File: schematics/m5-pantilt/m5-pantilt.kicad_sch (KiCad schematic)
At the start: 33 parts, among them J1 Conn_02x15_Odd_Even, J2 Conn_02x15_Odd_Even, J3 Conn_01x03, J4 Conn_01x04, J5 BAT, J6 Conn_01x04, J7 5V_POWER, J8 Conn_01x03, Q1 IRLML6402, Q2 2SA1015, SW1 SW_SPDT, U1 MAX3485

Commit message: WIP: Refine board
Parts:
- C1, C2, C3, C4: footprint Capacitor_SMD:C_1206_3216Metric_Pad1.42x1.75mm_HandSolder -> Capacitor_SMD:C_1206_3216Metric_Pad1.33x1.80mm_HandSolder
- Q2: footprint Package_TO_SOT_THT:TO-92_Inline -> Package_TO_SOT_SMD:SOT-23
- R10, R11, R12, R13, R14, R3, R4, R5, R9: footprint Resistor_SMD:R_0603_1608Metric_Pad1.05x0.95mm_HandSolder -> Resistor_SMD:R_0603_1608Metric_Pad0.98x0.95mm_HandSolder
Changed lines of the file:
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@@
       (effects (font (size 1.27 1.27)) (justify left))
     )
-    (property "Footprint" "Resistor_SMD:R_0603_1608Metric_Pad1.05x0.95mm_HandSolder" (id 2) (at 205.74 97.282 90)
+    (property "Footprint" "Resistor_SMD:R_0603_1608Metric_Pad0.98x0.95mm_HandSolder" (id 2) (at 205.74 97.282 90)
       (effects (font (size 1.27 1.27)) hide)
     )
@@
       (effects (font (size 1.27 1.27)) (justify left))
     )
-    (property "Footprint" "Resistor_SMD:R_0603_1608Metric_Pad1.05x0.95mm_HandSolder" (id 2) (at 205.74 123.952 90)
+    (property "Footprint" "Resistor_SMD:R_0603_1608Metric_Pad0.98x0.95mm_HandSolder" (id 2) (at 205.74 123.952 90)
       (effects (font (size 1.27 1.27)) hide)
     )
@@
     (property "Reference" "C1" (id 0) (at 215.9 86.36 0))
     (property "Value" "100u" (id 1) (at 214.63 88.9 0))
-    (property "Footprint" "Capacitor_SMD:C_1206_3216Metric_Pad1.42x1.75mm_HandSolder" (id 2) (at 218.7448 83.82 0)
+    (property "Footprint" "Capacitor_SMD:C_1206_3216Metric_Pad1.33x1.80mm_HandSolder" (id 2) (at 218.7448 83.82 0)
       (effects (font (size 1.27 1.27)) hide)
     )
@@
     (property "Reference" "C4" (id 0) (at 215.9 111.76 0))
     (property "Value" "100u" (id 1) (at 214.63 114.3 0))
-    (property "Footprint" "Capacitor_SMD:C_1206_3216Metric_Pad1.42x1.75mm_HandSolder" (id 2) (at 218.7448 109.22 0)
+    (property "Footprint" "Capacitor_SMD:C_1206_3216Metric_Pad1.33x1.80mm_HandSolder" (id 2) (at 218.7448 109.22 0)
       (effects (font (size 1.27 1.27)) hide)
     )
@@
       (effects (font (size 1.27 1.27)) (justify right))
     )
-    (property "Footprint" "Resistor_SMD:R_0603_1608Metric_Pad1.05x0.95mm_HandSolder" (id 2) (at 36.068 143.51 90)
+    (property "Footprint" "Resistor_SMD:R_0603_1608Metric_Pad0.98x0.95mm_HandSolder" (id 2) (at 36.068 143.51 90)
       (effects (font (size 1.27 1.27)) hide)
     )
@@
     (property "Reference" "C2" (id 0) (at 204.47 86.36 0))
     (property "Value" "100u" (id 1) (at 203.2 88.9 0))
-    (property "Footprint" "Capacitor_SMD:C_1206_3216Metric_Pad1.42x1.75mm_HandSolder" (id 2) (at 207.3148 83.82 0)
+    (property "Footprint" "Capacitor_SMD:C_1206_3216Metric_Pad1.33x1.80mm_HandSolder" (id 2) (at 207.3148 83.82 0)
       (effects (font (size 1.27 1.27)) hide)
     )
@@
     (property "Reference" "C3" (id 0) (at 204.47 111.76 0))
     (property "Value" "100u" (id 1) (at 203.2 114.3 0))
-    (property "Footprint" "Capacitor_SMD:C_1206_3216Metric_Pad1.42x1.75mm_HandSolder" (id 2) (at 209.2452 116.84 0)
+    (property "Footprint" "Capacitor_SMD:C_1206_3216Metric_Pad1.33x1.80mm_HandSolder" (id 2) (at 209.2452 116.84 0)
       (effects (font (size 1.27 1.27)) hide)
     )
@@
     (property "Reference" "R9" (id 0) (at 220.98 32.8422 90))
     (property "Value" "0" (id 1) (at 220.98 35.1536 90))
-    (property "Footprint" "Resistor_SMD:R_0603_1608Metric_Pad1.05x0.95mm_HandSolder" (id 2) (at 220.98 36.322 90)
+    (property "Footprint" "Resistor_SMD:R_0603_1608Metric_Pad0.98x0.95mm_HandSolder" (id 2) (at 220.98 36.322 90)
       (effects (font (size 1.27 1.27)) hide)
     )
@@
     (property "Reference" "R10" (id 0) (at 220.98 41.7322 90))
     (property "Value" "0" (id 1) (at 220.98 44.0436 90))
-    (property "Footprint" "Resistor_SMD:R_0603_1608Metric_Pad1.05x0.95mm_HandSolder" (id 2) (at 220.98 45.212 90)
+    (property "Footprint" "Resistor_SMD:R_0603_1608Metric_Pad0.98x0.95mm_HandSolder" (id 2) (at 220.98 45.212 90)
       (effects (font (size 1.27 1.27)) hide)
     )
@@
     (property "Reference" "R11" (id 0) (at 220.98 50.6222 90))
     (property "Value" "0" (id 1) (at 220.98 52.9336 90))
-    (property "Footprint" "Resistor_SMD:R_0603_1608Metric_Pad1.05x0.95mm_HandSolder" (id 2) (at 220.98 54.102 90)
+    (property "Footprint" "Resistor_SMD:R_0603_1608Metric_Pad0.98x0.95mm_HandSolder" (id 2) (at 220.98 54.102 90)
       (effects (font (size 1.27 1.27)) hide)
     )
@@
     (property "Reference" "R12" (id 0) (at 220.98 59.5122 90))
     (property "Value" "0" (id 1) (at 220.98 61.8236 90))
-    (property "Footprint" "Resistor_SMD:R_0603_1608Metric_Pad1.05x0.95mm_HandSolder" (id 2) (at 220.98 62.992 90)
+    (property "Footprint" "Resistor_SMD:R_0603_1608Metric_Pad0.98x0.95mm_HandSolder" (id 2) (at 220.98 62.992 90)
       (effects (font (size 1.27 1.27)) hide)
     )
@@
     (property "Reference" "R13" (id 0) (at 227.33 96.52 90))
     (property "Value" "0" (id 1) (at 229.87 96.1136 90))
-    (property "Footprint" "Resistor_SMD:R_0603_1608Metric_Pad1.05x0.95mm_HandSolder" (id 2) (at 229.87 97.282 90)
+    (property "Footprint" "Resistor_SMD:R_0603_1608Metric_Pad0.98x0.95mm_HandSolder" (id 2) (at 229.87 97.282 90)
       (effects (font (size 1.27 1.27)) hide)
     )
@@
     (property "Reference" "R14" (id 0) (at 227.33 123.19 90))
     (property "Value" "0" (id 1) (at 229.87 122.7836 90))
-    (property "Footprint" "Resistor_SMD:R_0603_1608Metric_Pad1.05x0.95mm_HandSolder" (id 2) (at 229.87 123.952 90)
+    (property "Footprint" "Resistor_SMD:R_0603_1608Metric_Pad0.98x0.95mm_HandSolder" (id 2) (at 229.87 123.952 90)
       (effects (font (size 1.27 1.27)) hide)
     )
@@
       (effects (font (size 1.27 1.27)) (justify left))
     )
-    (property "Footprint" "Package_TO_SOT_THT:TO-92_Inline" (id 2) (at 97.79 131.445 0)
+    (property "Footprint" "Package_TO_SOT_SMD:SOT-23" (id 2) (at 97.79 131.445 0)
       (effects (font (size 1.27 1.27) italic) (justify left) hide)
     )
@@
     )
     (path "/00000000-0000-0000-0000-000060cb98bd"
-      (reference "C1") (unit 1) (value "100u") (footprint "Capacitor_SMD:C_1206_3216Metric_Pad1.42x1.75mm_HandSolder")
+      (reference "C1") (unit 1) (value "100u") (footprint "Capacitor_SMD:C_1206_3216Metric_Pad1.33x1.80mm_HandSolder")
     )
     (path "/00000000-0000-0000-0000-000061ea93dc"
-      (reference "C2") (unit 1) (value "100u") (footprint "Capacitor_SMD:C_1206_3216Metric_Pad1.42x1.75mm_HandSolder")
+      (reference "C2") (unit 1) (value "100u") (footprint "Capacitor_SMD:C_1206_3216Metric_Pad1.33x1.80mm_HandSolder")
     )
     (path "/00000000-0000-0000-0000-000061eb9195"
-      (reference "C3") (unit 1) (value "100u") (footprint "Capacitor_SMD:C_1206_3216Metric_Pad1.42x1.75mm_HandSolder")
+      (reference "C3") (unit 1) (value "100u") (footprint "Capacitor_SMD:C_1206_3216Metric_Pad1.33x1.80mm_HandSolder")
     )
     (path "/00000000-0000-0000-0000-000061dd33e8"
-      (reference "C4") (unit 1) (value "100u") (footprint "Capacitor_SMD:C_1206_3216Metric_Pad1.42x1.75mm_HandSolder")
+      (reference "C4") (unit 1) (value "100u") (footprint "Capacitor_SMD:C_1206_3216Metric_Pad1.33x1.80mm_HandSolder")
     )
     (path "/00000000-0000-0000-0000-000064ba5a4b"
@@
     )
     (path "/00000000-0000-0000-0000-000064bdb211"
-      (reference "Q2") (unit 1) (value "2SA1015") (footprint "Package_TO_SOT_THT:TO-92_Inline")
+      (reference "Q2") (unit 1) (value "2SA1015") (footprint "Package_TO_SOT_SMD:SOT-23")
     )
     (path "/202ce841-9799-487b-99b7-75e313de629f"
@@
     )
     (path "/00000000-0000-0000-0000-000060c80000"
-      (reference "R3") (unit 1) (value "1k") (footprint "Resistor_SMD:R_0603_1608Metric_Pad1.05x0.95mm_HandSolder")
+      (reference "R3") (unit 1) (value "1k") (footprint "Resistor_SMD:R_0603_1608Metric_Pad0.98x0.95mm_HandSolder")
     )
     (path "/00000000-0000-0000-0000-000060c8863a"
-      (reference "R4") (unit 1) (value "1k") (footprint "Resistor_SMD:R_0603_1608Metric_Pad1.05x0.95mm_HandSolder")
+      (reference "R4") (unit 1) (value "1k") (footprint "Resistor_SMD:R_0603_1608Metric_Pad0.98x0.95mm_HandSolder")
     )
     (path "/00000000-0000-0000-0000-000061dec6ed"
-      (reference "R5") (unit 1) (value "47k") (footprint "Resistor_SMD:R_0603_1608Metric_Pad1.05x0.95mm_HandSolder")
+      (reference "R5") (unit 1) (value "47k") (footprint "Resistor_SMD:R_0603_1608Metric_Pad0.98x0.95mm_HandSolder")
     )
     (path "/d5da4752-cd55-4f6d-aea2-a0a9d2d835e7"
@@
     )
     (path "/00000000-0000-0000-0000-000062f00fd0"
-      (reference "R9") (unit 1) (value "0") (footprint "Resistor_SMD:R_0603_1608Metric_Pad1.05x0.95mm_HandSolder")
+      (reference "R9") (unit 1) (value "0") (footprint "Resistor_SMD:R_0603_1608Metric_Pad0.98x0.95mm_HandSolder")
     )
     (path "/00000000-0000-0000-0000-000062f2bcba"
-      (reference "R10") (unit 1) (value "0") (footprint "Resistor_SMD:R_0603_1608Metric_Pad1.05x0.95mm_HandSolder")
+      (reference "R10") (unit 1) (value "0") (footprint "Resistor_SMD:R_0603_1608Metric_Pad0.98x0.95mm_HandSolder")
     )
     (path "/00000000-0000-0000-0000-000062f42c81"
-      (reference "R11") (unit 1) (value "0") (footprint "Resistor_SMD:R_0603_1608Metric_Pad1.05x0.95mm_HandSolder")
+      (reference "R11") (unit 1) (value "0") (footprint "Resistor_SMD:R_0603_1608Metric_Pad0.98x0.95mm_HandSolder")
     )
     (path "/00000000-0000-0000-0000-000062f4da9d"
-      (reference "R12") (unit 1) (value "0") (footprint "Resistor_SMD:R_0603_1608Metric_Pad1.05x0.95mm_HandSolder")
+      (reference "R12") (unit 1) (value "0") (footprint "Resistor_SMD:R_0603_1608Metric_Pad0.98x0.95mm_HandSolder")
     )
     (path "/00000000-0000-0000-0000-000062f8bb17"
-      (reference "R13") (unit 1) (value "0") (footprint "Resistor_SMD:R_0603_1608Metric_Pad1.05x0.95mm_HandSolder")
+      (reference "R13") (unit 1) (value "0") (footprint "Resistor_SMD:R_0603_1608Metric_Pad0.98x0.95mm_HandSolder")
     )
     (path "/00000000-0000-0000-0000-000062f969a1"
-      (reference "R14") (unit 1) (value "0") (footprint "Resistor_SMD:R_0603_1608Metric_Pad1.05x0.95mm_HandSolder")
+      (reference "R14") (unit 1) (value "0") (footprint "Resistor_SMD:R_0603_1608Metric_Pad0.98x0.95mm_HandSolder")
     )
     (path "/00000000-0000-0000-0000-000064ba6374"

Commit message: WIP: update board
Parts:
- J3, J8: footprint Connector_PinHeader_2.54mm:PinHeader_1x03_P2.54mm_Vertical -> Connector_JST:JST_EH_B3B-EH-A_1x03_P2.50mm_Vertical
- Q2: footprint Package_TO_SOT_SMD:SOT-23 -> m5-pantilt:2SA1015_SOT-23
- R13, R14: footprint Resistor_SMD:R_0603_1608Metric_Pad0.98x0.95mm_HandSolder -> Resistor_SMD:R_0603_1608Metric
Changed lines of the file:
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@@
     (property "Reference" "R13" (id 0) (at 227.33 96.52 90))
     (property "Value" "0" (id 1) (at 229.87 96.1136 90))
-    (property "Footprint" "Resistor_SMD:R_0603_1608Metric_Pad0.98x0.95mm_HandSolder" (id 2) (at 229.87 97.282 90)
+    (property "Footprint" "Resistor_SMD:R_0603_1608Metric" (id 2) (at 229.87 97.282 90)
       (effects (font (size 1.27 1.27)) hide)
     )
@@
     (property "Reference" "R14" (id 0) (at 227.33 123.19 90))
     (property "Value" "0" (id 1) (at 229.87 122.7836 90))
-    (property "Footprint" "Resistor_SMD:R_0603_1608Metric_Pad0.98x0.95mm_HandSolder" (id 2) (at 229.87 123.952 90)
+    (property "Footprint" "Resistor_SMD:R_0603_1608Metric" (id 2) (at 229.87 123.952 90)
       (effects (font (size 1.27 1.27)) hide)
     )
@@
       (effects (font (size 1.27 1.27)) (justify left))
     )
-    (property "Footprint" "Package_TO_SOT_SMD:SOT-23" (id 2) (at 97.79 131.445 0)
+    (property "Footprint" "m5-pantilt:2SA1015_SOT-23" (id 2) (at 97.79 131.445 0)
       (effects (font (size 1.27 1.27) italic) (justify left) hide)
     )
@@
       (effects (font (size 1.27 1.27)) (justify left))
     )
-    (property "Footprint" "Connector_PinHeader_2.54mm:PinHeader_1x03_P2.54mm_Vertical" (id 2) (at 248.92 109.22 0)
+    (property "Footprint" "Connector_JST:JST_EH_B3B-EH-A_1x03_P2.50mm_Vertical" (id 2) (at 248.92 109.22 0)
       (effects (font (size 1.27 1.27)) hide)
     )
@@
       (effects (font (size 1.27 1.27)) (justify left))
     )
-    (property "Footprint" "Connector_PinHeader_2.54mm:PinHeader_1x03_P2.54mm_Vertical" (id 2) (at 248.92 83.82 0)
+    (property "Footprint" "Connector_JST:JST_EH_B3B-EH-A_1x03_P2.50mm_Vertical" (id 2) (at 248.92 83.82 0)
       (effects (font (size 1.27 1.27)) hide)
     )
@@
     )
     (path "/00000000-0000-0000-0000-000064d4e0a6"
-      (reference "J3") (unit 1) (value "Conn_01x03") (footprint "Connector_PinHeader_2.54mm:PinHeader_1x03_P2.54mm_Vertical")
+      (reference "J3") (unit 1) (value "Conn_01x03") (footprint "Connector_JST:JST_EH_B3B-EH-A_1x03_P2.50mm_Vertical")
     )
     (path "/00000000-0000-0000-0000-000060ca66e1"
@@
     )
     (path "/00000000-0000-0000-0000-000064d3a231"
-      (reference "J8") (unit 1) (value "Conn_01x03") (footprint "Connector_PinHeader_2.54mm:PinHeader_1x03_P2.54mm_Vertical")
+      (reference "J8") (unit 1) (value "Conn_01x03") (footprint "Connector_JST:JST_EH_B3B-EH-A_1x03_P2.50mm_Vertical")
     )
     (path "/00000000-0000-0000-0000-000061ddc391"
@@
     )
     (path "/00000000-0000-0000-0000-000064bdb211"
-      (reference "Q2") (unit 1) (value "2SA1015") (footprint "Package_TO_SOT_SMD:SOT-23")
+      (reference "Q2") (unit 1) (value "2SA1015") (footprint "m5-pantilt:2SA1015_SOT-23")
     )
     (path "/202ce841-9799-487b-99b7-75e313de629f"
@@
     )
     (path "/00000000-0000-0000-0000-000062f8bb17"
-      (reference "R13") (unit 1) (value "0") (footprint "Resistor_SMD:R_0603_1608Metric_Pad0.98x0.95mm_HandSolder")
+      (reference "R13") (unit 1) (value "0") (footprint "Resistor_SMD:R_0603_1608Metric")
     )
     (path "/00000000-0000-0000-0000-000062f969a1"
-      (reference "R14") (unit 1) (value "0") (footprint "Resistor_SMD:R_0603_1608Metric_Pad0.98x0.95mm_HandSolder")
+      (reference "R14") (unit 1) (value "0") (footprint "Resistor_SMD:R_0603_1608Metric")
     )
     (path "/00000000-0000-0000-0000-000064ba6374"

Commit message: Update board
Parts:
- removed Q2: 2SA1015, m5-pantilt:2SA1015_SOT-23, symbol Transistor_BJT:2SA1015
- added Q2: BC857, Package_TO_SOT_SMD:SOT-23, symbol Transistor_BJT:BC857
- R2: value 7.5k -> 5k
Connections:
- net +3V3: now also Q2.2 (E)
- net at R7.1, U1.2 (~{RE}), U1.3 (DE): now also Q2.3 (C)
- net at R2.2: now also Q2.1 (B)
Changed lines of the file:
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@@
     (pin "1")
-  )
-  (symbol (lib_id "Transistor_BJT:2SA1015") (at 92.71 129.54 0) (unit 1)
-    (in_bom yes) (on_board yes)
-    (property "Reference" "Q2" (id 0) (at 97.5614 128.3716 0)
-      (effects (font (size 1.27 1.27)) (justify left))
-    )
-    (property "Value" "2SA1015" (id 1) (at 97.5614 130.683 0)
-      (effects (font (size 1.27 1.27)) (justify left))
-    )
-    (property "Footprint" "m5-pantilt:2SA1015_SOT-23" (id 2) (at 97.79 131.445 0)
-      (effects (font (size 1.27 1.27) italic) (justify left) hide)
-    )
-    (property "Datasheet" "http://www.datasheetcatalog.org/datasheet/toshiba/905.pdf" (id 3) (at 92.71 129.54 0)
-      (effects (font (size 1.27 1.27)) (justify left) hide)
-    )
-    (pin "1")
-    (pin "2")
-    (pin "3")
   )
   (symbol (lib_id "Device:R") (at 95.25 146.05 0) (unit 1)
@@
     (in_bom yes) (on_board yes) (fields_autoplaced)
     (property "Reference" "R2" (id 0) (at 81.28 123.19 90))
-    (property "Value" "7.5k" (id 1) (at 81.28 125.73 90))
+    (property "Value" "5k" (id 1) (at 81.28 125.73 90))
     (property "Footprint" "Resistor_SMD:R_0603_1608Metric" (id 2) (at 81.28 131.318 90)
       (effects (font (size 1.27 1.27)) hide)
@@
     (pin "1")
   )
+  (symbol (lib_id "Transistor_BJT:BC857") (at 92.71 129.54 0) (mirror x) (unit 1)
+    (in_bom yes) (on_board yes) (fields_autoplaced)
+    (property "Reference" "Q2" (id 0) (at 97.79 128.2699 0)
+      (effects (font (size 1.27 1.27)) (justify left))
+    )
+    (property "Value" "BC857" (id 1) (at 97.79 130.8099 0)
+      (effects (font (size 1.27 1.27)) (justify left))
+    )
+    (property "Footprint" "Package_TO_SOT_SMD:SOT-23" (id 2) (at 97.79 127.635 0)
+      (effects (font (size 1.27 1.27) italic) (justify left) hide)
+    )
+    (property "Datasheet" "https://www.onsemi.com/pub/Collateral/BC860-D.pdf" (id 3) (at 92.71 129.54 0)
+      (effects (font (size 1.27 1.27)) (justify left) hide)
+    )
+    (pin "1")
+    (pin "2")
+    (pin "3")
+  )
   (sheet_instances
     (path "/" (page "1"))
@@
       (reference "Q1") (unit 1) (value "IRLML6402") (footprint "Package_TO_SOT_SMD:SOT-23")
     )
-    (path "/00000000-0000-0000-0000-000064bdb211"
-      (reference "Q2") (unit 1) (value "2SA1015") (footprint "m5-pantilt:2SA1015_SOT-23")
+    (path "/fd72c6fd-8d01-4c84-aa64-052ccdf03377"
+      (reference "Q2") (unit 1) (value "BC857") (footprint "Package_TO_SOT_SMD:SOT-23")
     )
     (path "/202ce841-9799-487b-99b7-75e313de629f"
@@
     )
     (path "/b82df952-3fb3-4e09-9ff8-6b87cc7e46fc"
-      (reference "R2") (unit 1) (value "7.5k") (footprint "Resistor_SMD:R_0603_1608Metric")
+      (reference "R2") (unit 1) (value "5k") (footprint "Resistor_SMD:R_0603_1608Metric")
     )
     (path "/00000000-0000-0000-0000-000060c80000"

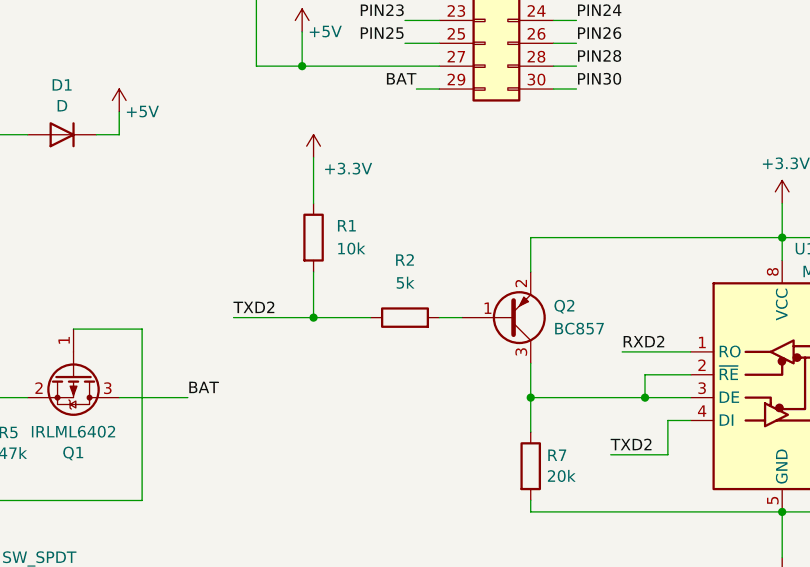
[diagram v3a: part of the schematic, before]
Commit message: 5k->5.1k
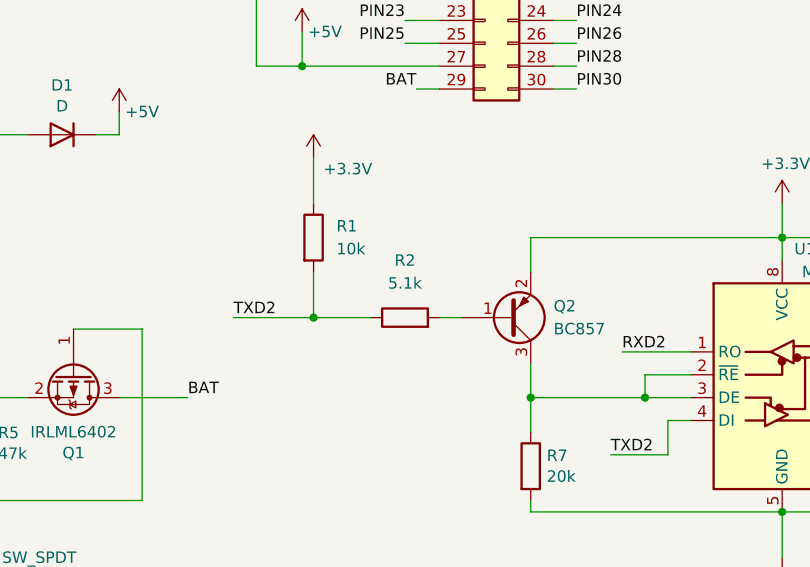
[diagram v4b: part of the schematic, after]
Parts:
- R2: value 5k -> 5.1k
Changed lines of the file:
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@@
     (in_bom yes) (on_board yes) (fields_autoplaced)
     (property "Reference" "R2" (id 0) (at 81.28 123.19 90))
-    (property "Value" "5k" (id 1) (at 81.28 125.73 90))
+    (property "Value" "5.1k" (id 1) (at 81.28 125.73 90))
     (property "Footprint" "Resistor_SMD:R_0603_1608Metric" (id 2) (at 81.28 131.318 90)
       (effects (font (size 1.27 1.27)) hide)
@@
     )
     (path "/b82df952-3fb3-4e09-9ff8-6b87cc7e46fc"
-      (reference "R2") (unit 1) (value "5k") (footprint "Resistor_SMD:R_0603_1608Metric")
+      (reference "R2") (unit 1) (value "5.1k") (footprint "Resistor_SMD:R_0603_1608Metric")
     )
     (path "/00000000-0000-0000-0000-000060c80000"

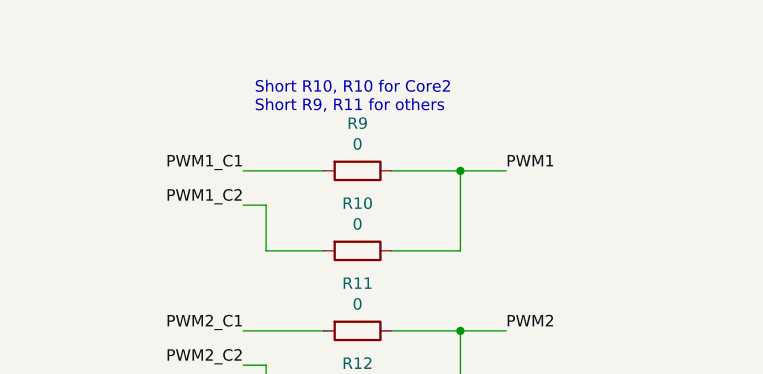
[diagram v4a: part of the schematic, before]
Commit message: Upgrade to KiCad 7
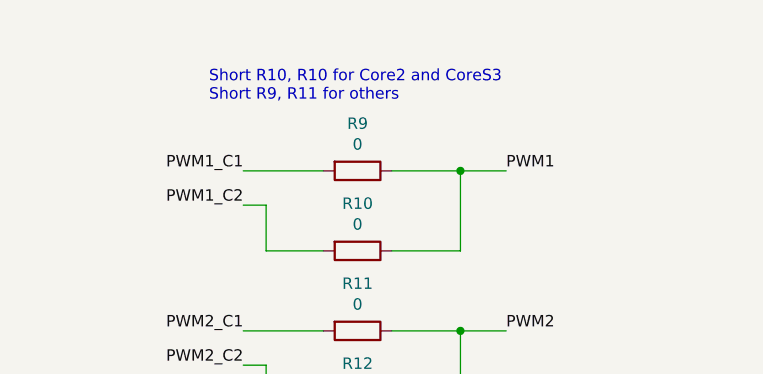
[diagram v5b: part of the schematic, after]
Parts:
- J5: LCSC (none) -> C2319
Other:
- note added: "Short R10, R10 for Core2 and CoreS3 Short R9, R11 for others"
- note removed: "Short R10, R10 for Core2 Short R9, R11 for others"
